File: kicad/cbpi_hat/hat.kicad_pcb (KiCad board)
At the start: 2 copper layers, 65 x 56 mm, 5 parts, among them J1 GPIO

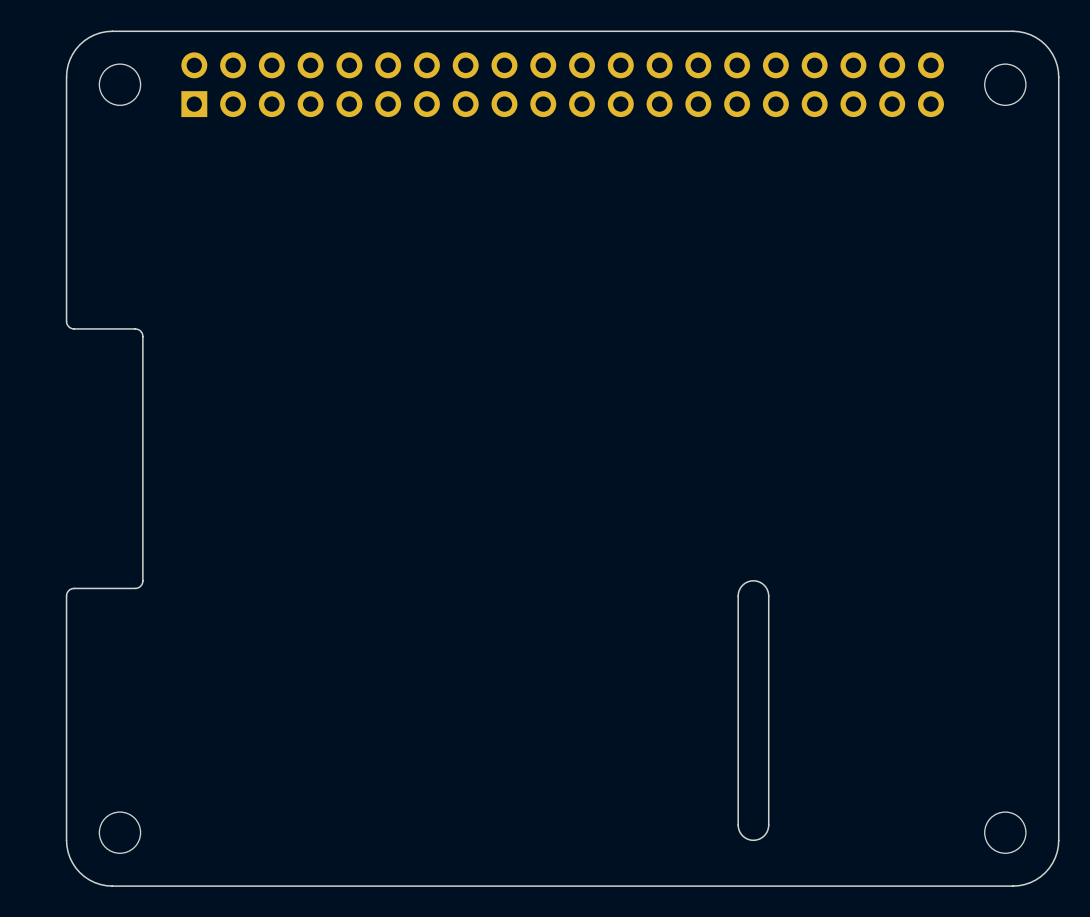
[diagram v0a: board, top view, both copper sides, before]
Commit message: Placed first components on board, no routing yet
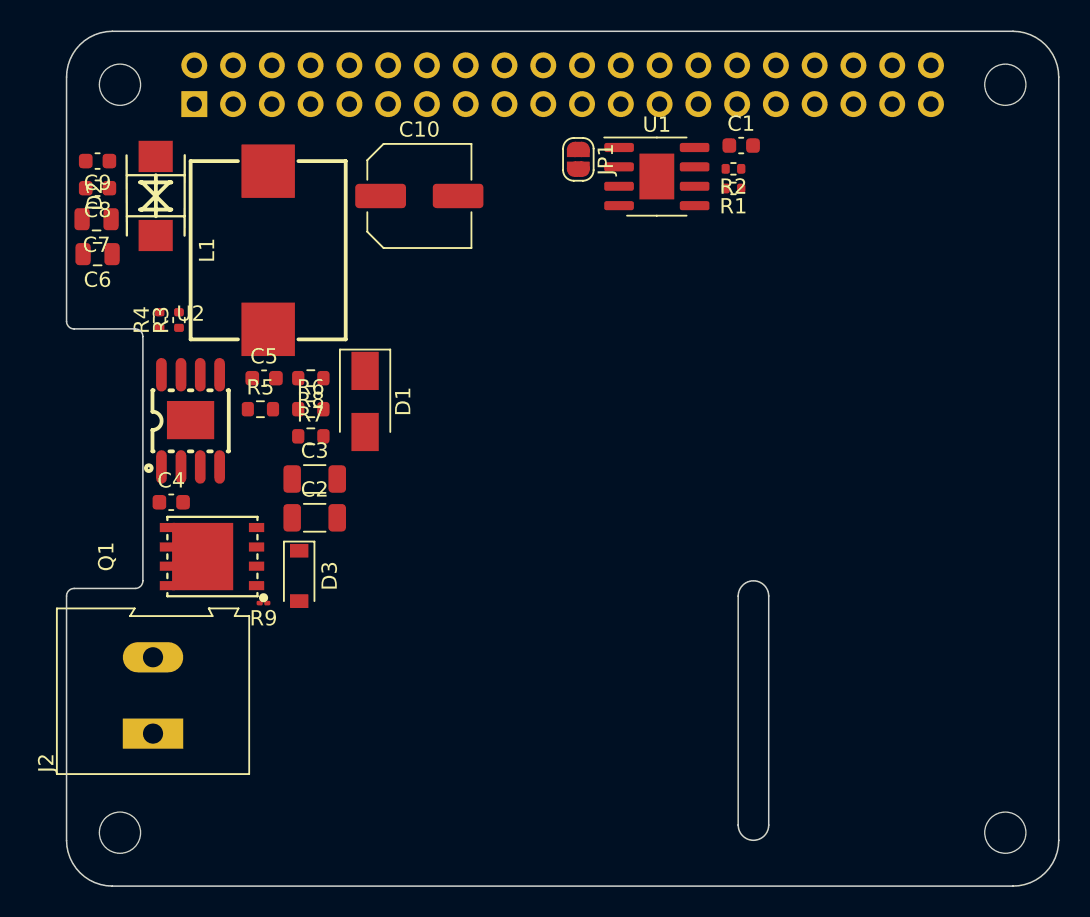
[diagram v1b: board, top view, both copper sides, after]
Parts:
- added C1: 100n, Capacitor_SMD:C_0603_1608Metric, F.Cu at (144.2, 51.5)
- added C10: 220uF, Capacitor_SMD:C_Elec_6.3x5.4, F.Cu at (123.1, 54.8)
- added C2: 10uF, Capacitor_SMD:C_1206_3216Metric, F.Cu at (116.3, 75.9)
- added C3: 10uF, Capacitor_SMD:C_1206_3216Metric, F.Cu at (116.3, 73.3)
- added C4: 10nF, Capacitor_SMD:C_0603_1608Metric, F.Cu at (106.9, 74.9)
- added C5: 1.5nF, Capacitor_SMD:C_0603_1608Metric, F.Cu at (112.9, 66.7)
- added C6: 22uF, Capacitor_SMD:C_0805_2012Metric, F.Cu at (102.0, 58.6)
- added C7: 22uF, Capacitor_SMD:C_0805_2012Metric, F.Cu at (102.0, 56.3)
- added C8: 1nF, Capacitor_SMD:C_0603_1608Metric, F.Cu at (102.0, 54.3)
- added C9: 100nF, Capacitor_SMD:C_0603_1608Metric, F.Cu at (102.0, 52.5)
- added D1: B340, Diode_SMD:D_SMA, F.Cu at (119.6, 68.2)
- added D2: SMBJ5.0CA-TP, smbj5.0ca-tp:SMB_L4.6-W3.6-LS5.3-BI, F.Cu at (105.8, 54.8)
- added D3: MM1Z9V1, Diode_SMD:D_SOD-123, F.Cu at (115.2, 79.7)
- added J2: Screw_Terminal_01x02, TerminalBlock:TerminalBlock_Altech_AK300-2_P5.00mm, F.Cu at (105.7, 90.0)
- added JP1: ID_WP, Jumper:SolderJumper-2_P1.3mm_Open_RoundedPad1.0x1.5mm, F.Cu at (133.5, 52.4)
- added L1: 33uH, SMMS1050-330M:IND-SMD_L11.5-W10.0, F.Cu at (113.2, 58.3)
- added Q1: HY15P03C2, hy15p03c2:DFN-8_L5.9-W5.2-P1.27-LS6.2-BL, F.Cu at (109.5, 78.4)
- added R1: 3.9k, Resistor_SMD:R_0402_1005Metric, F.Cu at (143.7, 54.3)
- added R2: 3.9k, Resistor_SMD:R_0402_1005Metric, F.Cu at (143.7, 53.0)
- added R3: 44.2k, Resistor_SMD:R_0402_1005Metric, F.Cu at (107.4, 62.9)
- added R4: 200k, Resistor_SMD:R_0402_1005Metric, F.Cu at (106.1, 62.9)
- added R5: 10k, Resistor_SMD:R_0603_1608Metric, F.Cu at (112.7, 68.8)
- added R6: 43k, Resistor_SMD:R_0603_1608Metric, F.Cu at (116.0, 68.8)
- added R7: 10k, Resistor_SMD:R_0603_1608Metric, F.Cu at (116.0, 70.5)
- added R8: 10k, Resistor_SMD:R_0603_1608Metric, F.Cu at (116.0, 66.7)
- added R9: 100, Resistor_SMD:R_01005_0402Metric, F.Cu at (112.9, 81.5)
- added U1: CAT24C256, Package_SO:SOIC-8-1EP_3.9x4.9mm_P1.27mm_EP2.29x3mm, F.Cu at (138.7, 53.5)
- added U2: EUP3453WIR1, eup3453wir1:SOIC-8_L4.9-W3.9-P1.27-LS6.0-BL-EP3.1, F.Cu at (108.1, 69.5)
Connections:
- net +3V3 renamed +3.3V

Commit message: 5V DC-DC converter is largely routed including reverse polarity protection
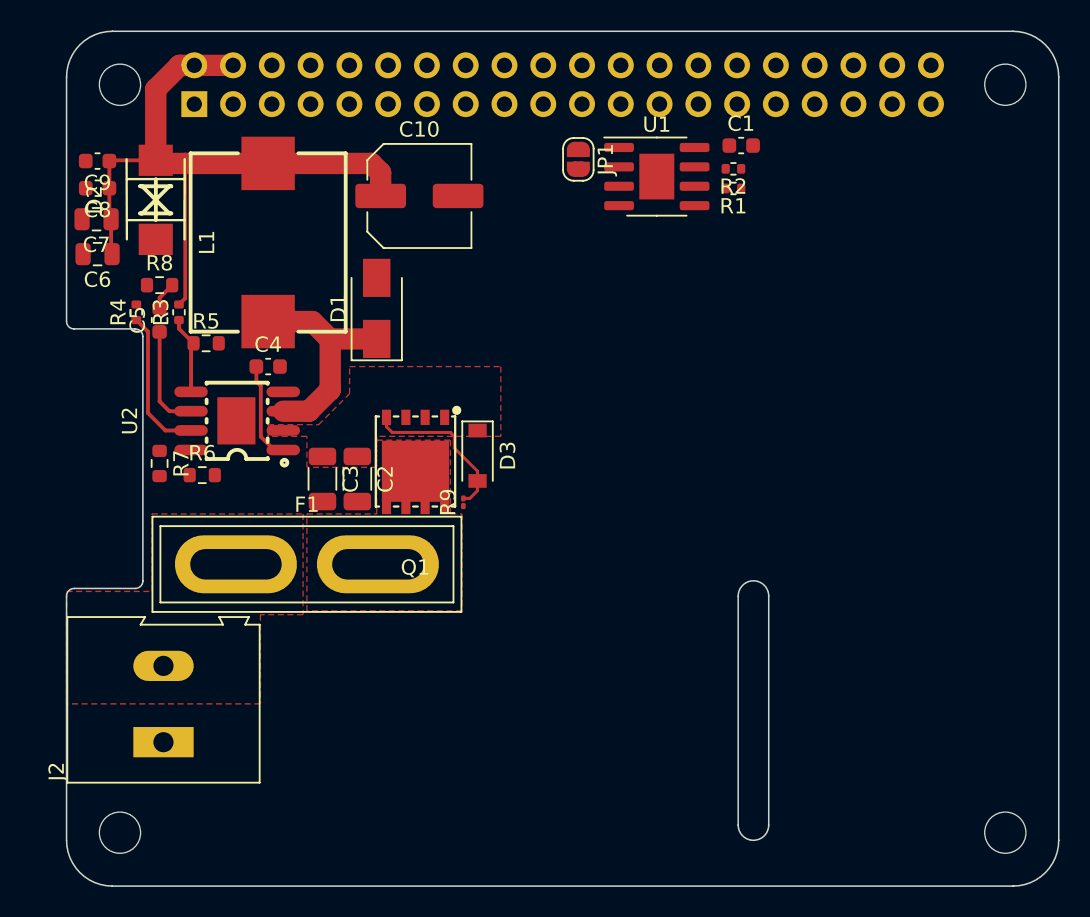
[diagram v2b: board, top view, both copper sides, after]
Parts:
- added F1: Fuse, Fuse:Fuse_Blade_ATO_directSolder, F.Cu at (111.1, 78.9)
- moved Q1 14.7 mm to (122.9, 72.2), turned to 180 degrees
- moved R9 14.7 mm to (126.0, 74.9), turned to 90 degrees
- moved D3 14.1 mm to (126.9, 71.8)
- moved R8 11.6 mm to (106.1, 60.6), turned to 0 degrees
- moved C4 10.9 mm to (113.2, 66.0)
- moved R7 10.1 mm to (106.1, 72.3), turned to -90 degrees
- moved R6 8.32 mm to (108.9, 73.1)
- moved C5 7.83 mm to (106.1, 62.9), turned to 90 degrees
- moved D1 6.14 mm to (120.3, 62.2), turned to 90 degrees
- moved R5 5.59 mm to (109.1, 64.4)
- moved C2 3.78 mm to (119.0, 73.3), turned to -90 degrees
- moved U2 3.05 mm to (111.2, 69.5), turned to 90 degrees
- moved R4 1.61 mm to (104.6, 62.4)
- moved J2 0.89 mm to (106.3, 90.6)
- moved L1 0.51 mm to (113.2, 57.8)
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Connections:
- net Net-(C4-Pad2) renamed /PWR_5V_SW_OUT
- J2 pad 2: Net-(J2-Pad2) -> /24V_PRE_FUSE
- Q1 pad 5: Net-(J2-Pad2) -> /24V_PRE_PP
- Q1 pad 6: Net-(J2-Pad2) -> /24V_PRE_PP
- Q1 pad 7: Net-(J2-Pad2) -> /24V_PRE_PP
- Q1 pad 8: Net-(J2-Pad2) -> /24V_PRE_PP
- Q1 pad 9: Net-(J2-Pad2) -> /24V_PRE_PP
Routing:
- net +5V: track 0.00 -> 45.7 mm
- net /PWR_5V_SW_OUT: track 0.00 -> 14.6 mm
- net Net-(D3-Pad2): track 0.00 -> 10.6 mm
- net Net-(R4-Pad1): track 0.00 -> 9.70 mm
- net Net-(C5-Pad1): track 0.00 -> 6.88 mm
- net Net-(C4-Pad1): track 0.00 -> 6.55 mm
- net Net-(R3-Pad1): track 0.00 -> 5.16 mm
- net Net-(C5-Pad2): track 0.00 -> 1.85 mm
- added copper zone on F.Cu, net +24V
- added copper zone on F.Cu, net /24V_PRE_FUSE
- added copper zone on F.Cu, net /24V_PRE_PP

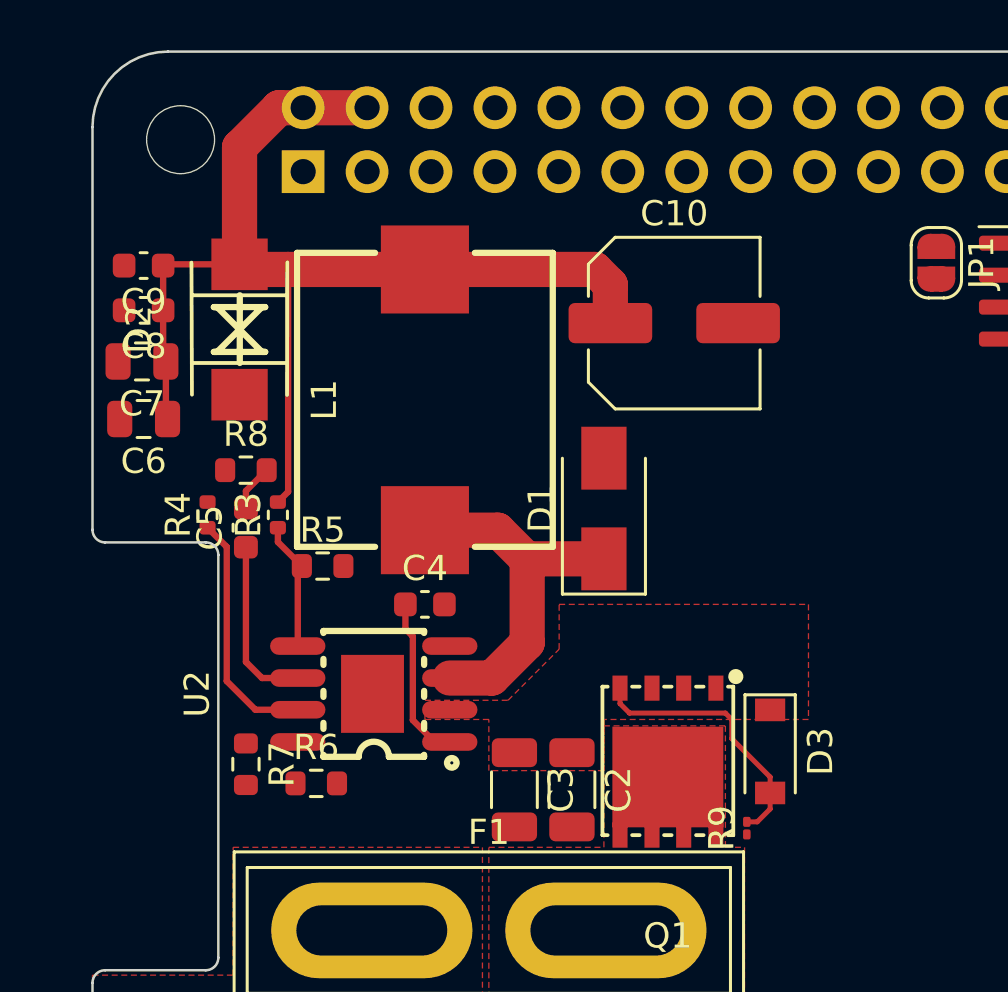
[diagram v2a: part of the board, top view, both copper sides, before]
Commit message: Added protection against back powering. This should fix #12
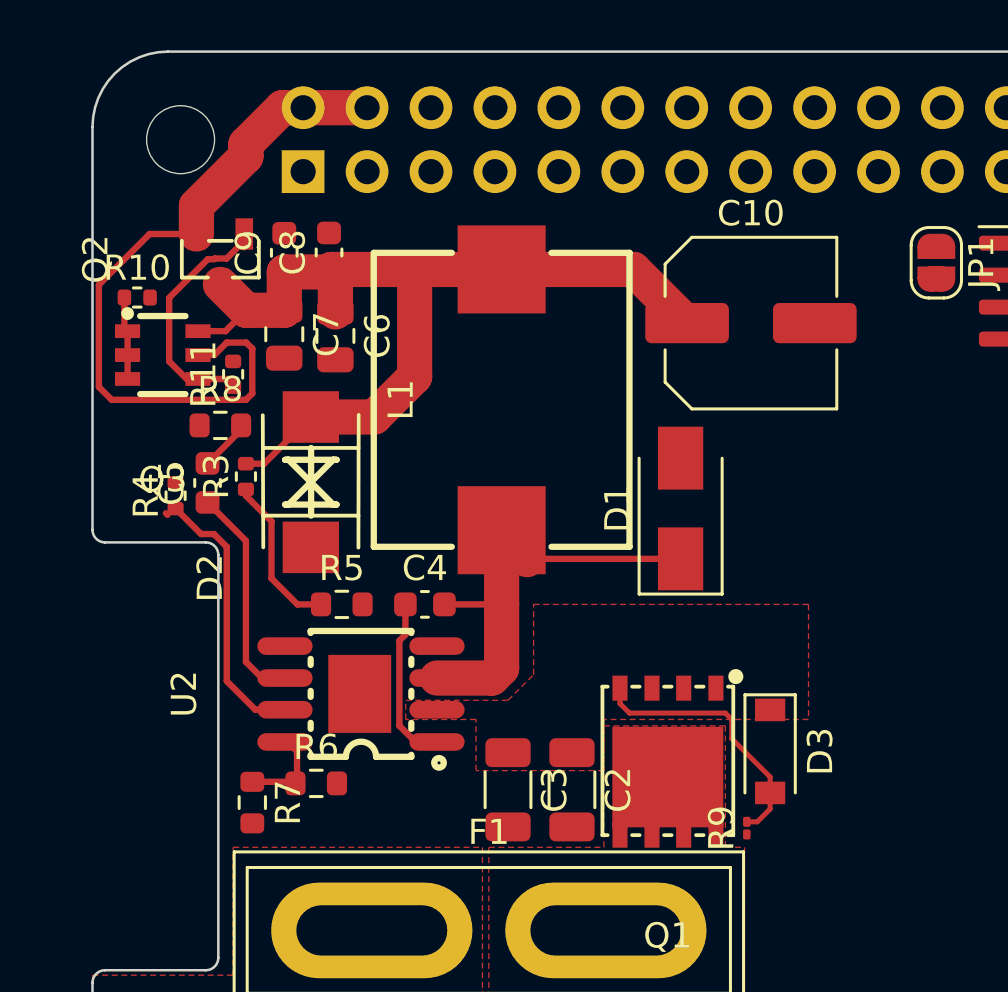
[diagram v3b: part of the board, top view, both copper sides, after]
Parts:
- added Q2: DMG2305UX, dmg2305ux:SOT-23-3_L2.9-W1.3-P0.95-LS2.4-BR-1, F.Cu at (105.1, 52.2)
- added Q3: DMMT5401-7-F, dmmt5401-f-7:SOT-23-6_L2.9-W1.6-P0.95-LS2.8-BR, F.Cu at (102.8, 56.1)
- added R10: 10k, Resistor_SMD:R_0402_1005Metric, F.Cu at (101.8, 53.8)
- added R11: 47k, Resistor_SMD:R_0402_1005Metric, F.Cu at (105.6, 56.8)
- moved C6 8.30 mm to (109.7, 55.3), turned to -90 degrees
- moved C8 7.72 mm to (109.4, 52.0), turned to 90 degrees
- moved D2 6.70 mm to (108.7, 61.1)
- moved C7 5.76 mm to (107.6, 55.2), turned to -90 degrees
- moved C9 5.61 mm to (107.6, 52.0), turned to 90 degrees
- moved C10 3.05 mm to (126.2, 54.8)
- moved D1 3.05 mm to (123.4, 62.2)
- moved L1 3.05 mm to (116.3, 57.8)
- moved C5 2.34 mm to (104.6, 61.1)
- moved R8 2.05 mm to (105.1, 58.9)
- moved R3 1.98 mm to (106.1, 60.9)
- moved R5 1.70 mm to (109.9, 66.0)
- moved R7 1.55 mm to (106.3, 73.8)
- moved R4 1.48 mm to (103.3, 61.6)
- moved U2 0.51 mm to (110.7, 69.5)
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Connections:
- J1 pad 2: +5V -> +5VD
- J1 pad 4: +5V -> +5VD
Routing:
- net +5VD: track 0.00 -> 29.2 mm
- net Net-(Q2-Pad1): track 0.00 -> 10.1 mm
- net +5V: track 45.7 -> 38.1 mm
- net Net-(R6-Pad1): track 0.00 -> 3.67 mm
- net /PWR_5V_SW_OUT: track 14.6 -> 18.1 mm
- net Net-(Q3-Pad1): track 0.00 -> 3.29 mm
- net Net-(C5-Pad1): track 6.88 -> 9.29 mm
- net Net-(R4-Pad1): track 9.70 -> 11.4 mm
- net Net-(R3-Pad1): track 5.16 -> 6.36 mm
- net Net-(C4-Pad1): track 6.55 -> 7.28 mm

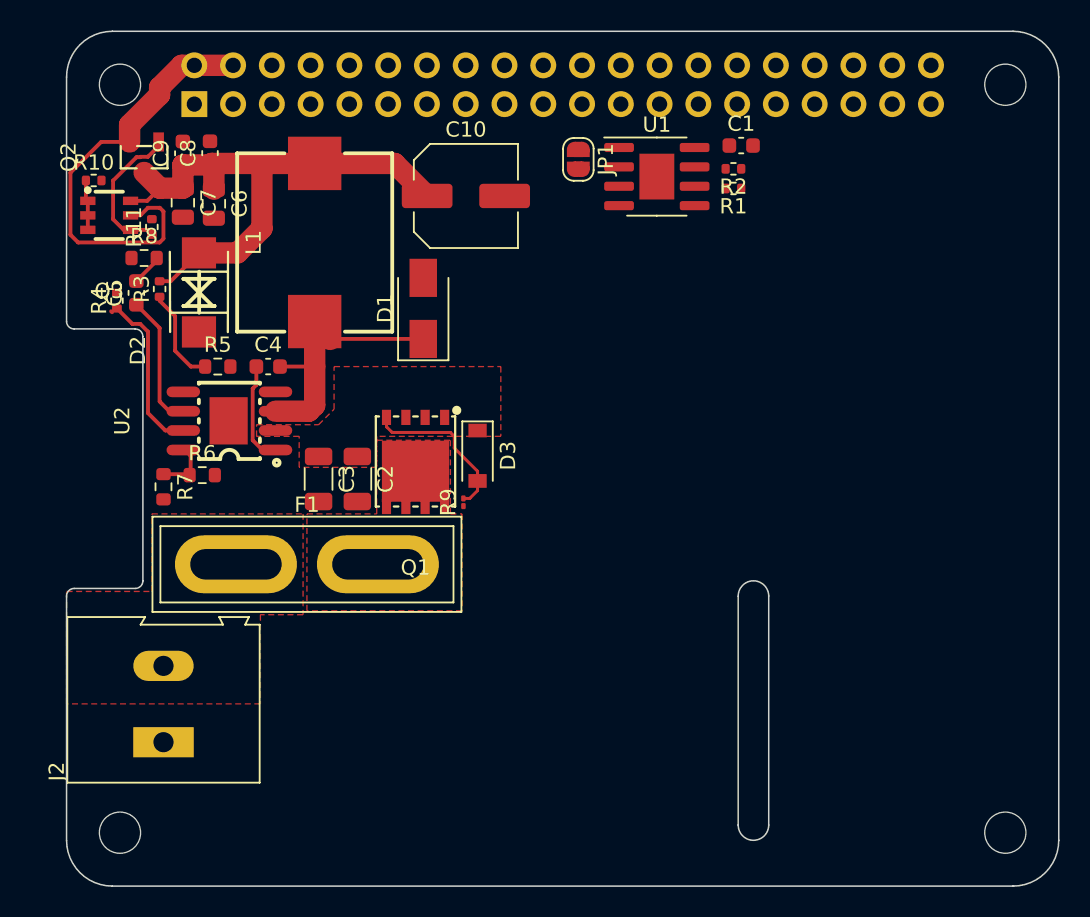
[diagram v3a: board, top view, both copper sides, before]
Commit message: DC-DC converter and identity eeprom should be fully routed now (except for GND).
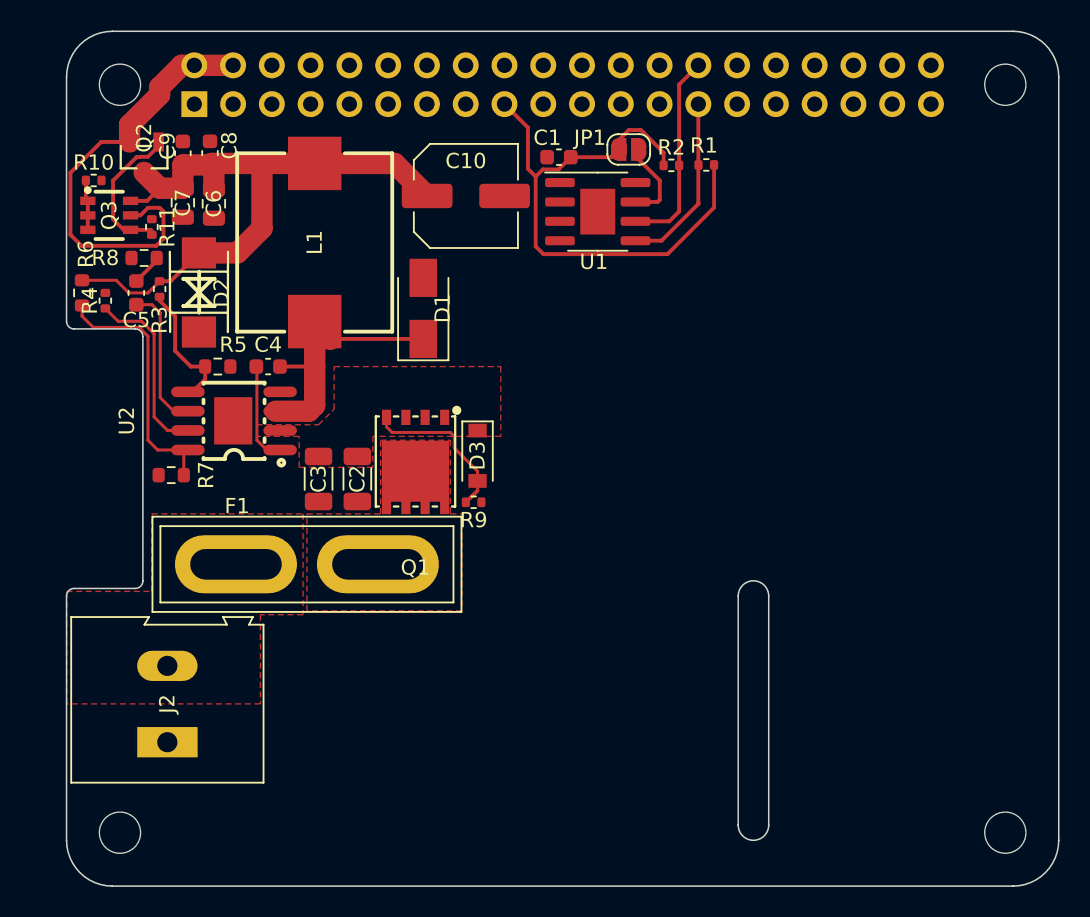
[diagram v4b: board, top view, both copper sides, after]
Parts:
- R9: footprint Resistor_SMD:R_01005_0402Metric -> Resistor_SMD:R_0402_1005Metric
- moved R6 14.3 mm to (101.0, 61.1), turned to 90 degrees
- moved C1 12.0 mm to (132.3, 52.2), turned to 180 degrees
- moved U1 4.50 mm to (134.8, 55.8)
- moved R2 4.07 mm to (139.6, 52.8), turned to 0 degrees
- moved JP1 3.37 mm to (136.8, 51.7), turned to 180 degrees
- moved R1 2.35 mm to (141.9, 52.8)
- moved R7 0.92 mm to (106.9, 73.1), turned to 180 degrees
- moved R4 0.76 mm to (102.5, 61.6)
- moved R9 0.67 mm to (126.7, 74.9), turned to 180 degrees
- moved U2 0.30 mm to (111.0, 69.5)
- moved J2 0.25 mm to (106.6, 90.6)
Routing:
- net +3.3V: track 0.00 -> 38.6 mm
- net Net-(R6-Pad1): track 3.67 -> 17.1 mm
- net /ID_SCL: track 0.00 -> 13.4 mm
- net /ID_SDA: track 0.00 -> 11.9 mm
- net +5V: track 38.1 -> 43.8 mm
- net Net-(JP1-Pad1): track 0.00 -> 5.52 mm
- net Net-(R3-Pad1): track 6.36 -> 8.96 mm
- net Net-(R4-Pad1): track 11.4 -> 11.9 mm
